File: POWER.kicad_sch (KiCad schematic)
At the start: 44 parts, among them U4 LMR43620R5RPER, U5 LMR604303SRAKRQ1, U6 AP7361C-33FGE-7, U7 AP7361C-33FGE-7

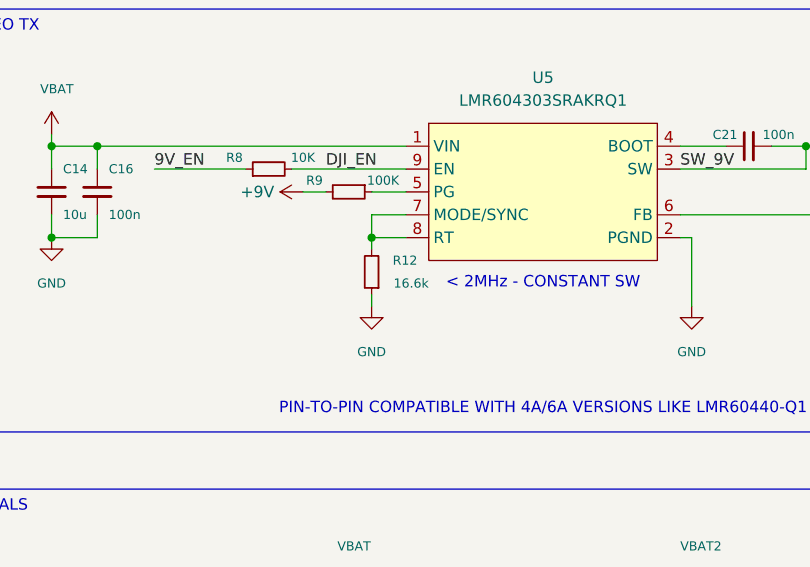
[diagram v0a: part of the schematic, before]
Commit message: BOM LCSC numbers assigned
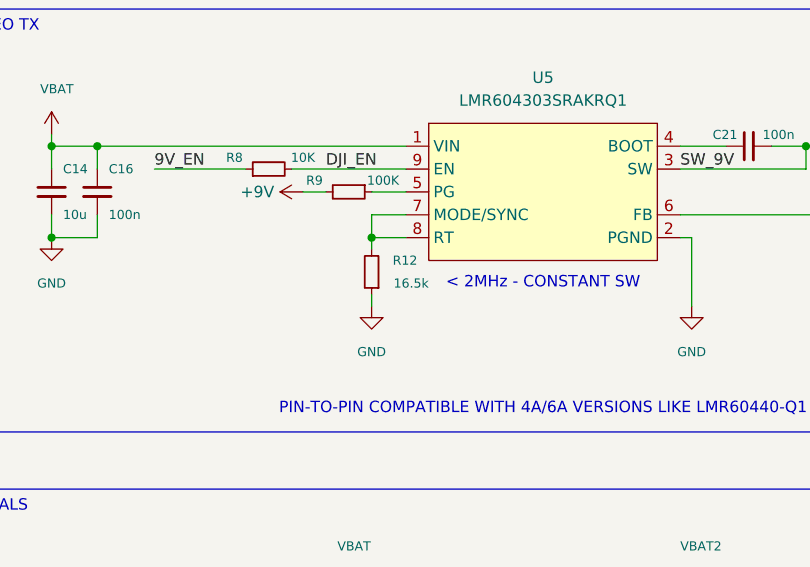
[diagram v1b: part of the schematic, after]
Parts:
- C13, C14: LCSC Part (none) -> C440198
- C15, C16, C17, C20, C21, C26, C28: LCSC Part (none) -> C1525
- C18: LCSC Part (none) -> C15849
- C22, C24, C25, C27: LCSC Part (none) -> C45783
- C29, C30, C31, C32: LCSC Part (none) -> C19666
- D2: LCSC Part (none) -> C134980
- D3, D4: LCSC Part (none) -> C2905650
- L1, L2: LCSC Part (none) -> C6012410
- R10, R19, R20, R8: LCSC Part (none) -> C25744
- R11: LCSC Part (none) -> C11702
- R12: value 16.6k -> 16.5k; LCSC Part (none) -> C25857
- R15, R9: LCSC Part (none) -> C25741
- R16: LCSC Part (none) -> C11692
